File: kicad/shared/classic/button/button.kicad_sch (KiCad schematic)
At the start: 0 parts

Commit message: Draft of Classic button/LED assembly
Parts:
- added D1: LED, LED_THT:LED_D5.0mm, symbol Device:LED
- added J2: Screw_Terminal_01x03, TerminalBlock_Phoenix:TerminalBlock_Phoenix_MKDS-1,5-3-5.08_1x03_P5.08mm_Horizontal, symbol Connector:Screw_Terminal_01x03
- added MX1: MX_SW_HS, PCM_marbastlib-mx:SW_MX_HS_CPG151101S11_1u, symbol marbastlib-mx:MX_SW_HS_CPG151101S11
- added Q1: BC547, Package_TO_SOT_THT:TO-92_Inline, symbol Transistor_BJT:BC547
- added R1: 180, Resistor_SMD:R_0805_2012Metric, symbol Device:R
- added R2: 1.3k, Resistor_SMD:R_0805_2012Metric, symbol Device:R
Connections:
- new net: D1.1 (K), Q1.1 (C)
- new net: D1.2 (A), R1.2
- new net: Q1.2 (B), R2.2
- new net +3V3: J2.1 (Pin_1), MX1.1, R1.1
- new net GND: J2.3 (Pin_3), Q1.3 (E)
- new net SW_OUT: J2.2 (Pin_2), MX1.2, R2.1

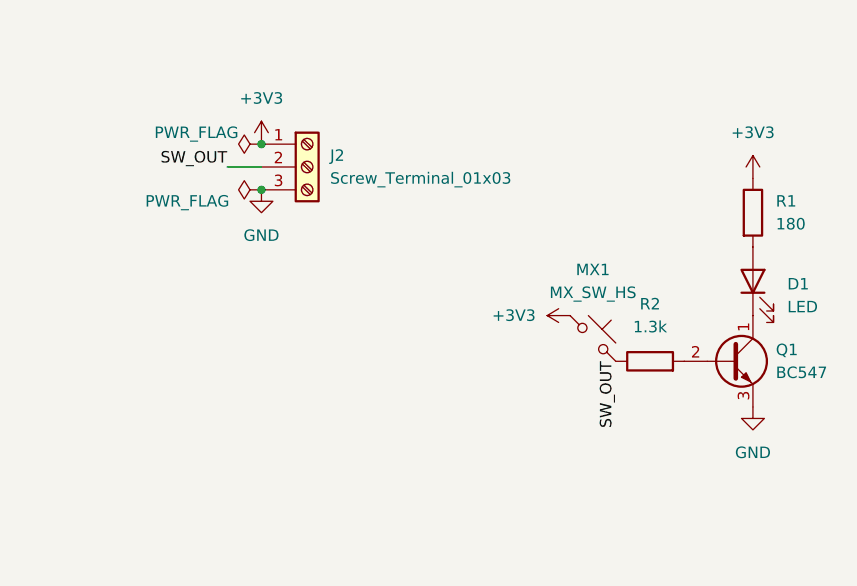
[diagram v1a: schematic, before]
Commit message: Decoupling cap and JST-XA connector for Classic button daughterboard
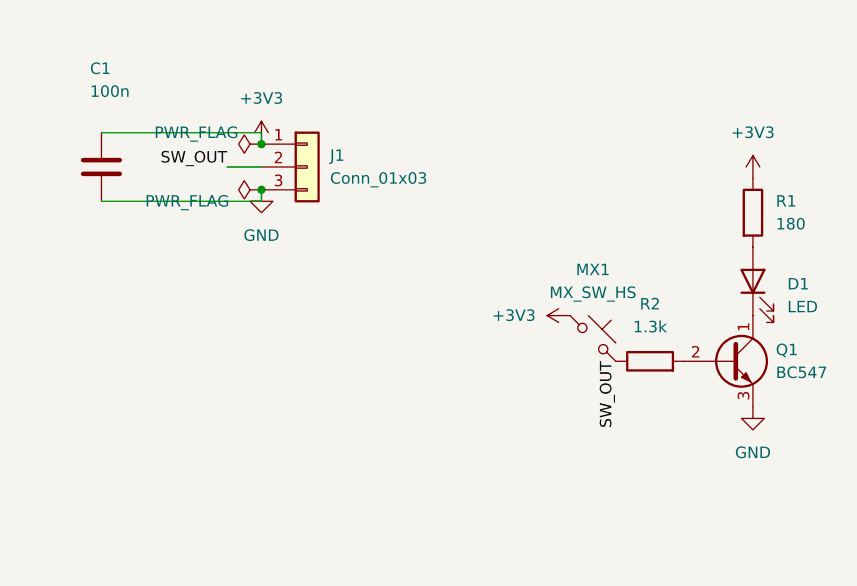
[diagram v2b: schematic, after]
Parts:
- removed J2: Screw_Terminal_01x03, TerminalBlock_Phoenix:TerminalBlock_Phoenix_MKDS-1,5-3-5.08_1x03_P5.08mm_Horizontal, symbol Connector:Screw_Terminal_01x03
- added C1: 100n, Capacitor_SMD:C_0805_2012Metric, symbol Device:C
- added J1: Conn_01x03, Connector_JST:JST_XA_S03B-XASK-1_1x03_P2.50mm_Horizontal, symbol Connector_Generic:Conn_01x03
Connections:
- net +3V3: now also C1.1, J1.1 (Pin_1)
- net GND: now also C1.2, J1.3 (Pin_3)
- net SW_OUT: now also J1.2 (Pin_2)
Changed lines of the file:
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@@
+	(wire
+		(pts
+			(xy 21.59 54.61) (xy 39.37 54.61)
+		)
+		(stroke
+			(width 0)
+			(type default)
+		)
+	)
+	(wire
+		(pts
+			(xy 39.37 60.96) (xy 39.37 62.23)
+		)
+		(stroke
+			(width 0)
+			(type default)
+		)
+	)
+	(wire
+		(pts
+			(xy 39.37 54.61) (xy 39.37 55.88)
+		)
+		(stroke
+			(width 0)
+			(type default)
+		)
+	)
 	(wire
 		(pts
 			(xy 35.56 58.42) (xy 39.37 58.42)
+		)
+		(stroke
+			(width 0)
+			(type default)
+		)
+	)
+	(wire
+		(pts
+			(xy 39.37 62.23) (xy 21.59 62.23)
 		)
 		(stroke
@@
 	)
 	(symbol
+		(lib_id "Device:C")
+		(at 21.59 58.42 0)
+		(unit 1)
+		(body_style 1)
+		(exclude_from_sim no)
+		(in_bom yes)
+		(on_board yes)
+		(in_pos_files yes)
+		(dnp no)
+		(property "Reference" "C1"
+			(at 20.32 47.498 0)
+			(show_name no)
+			(do_not_autoplace no)
+			(effects
+				(font
+					(size 1.27 1.27)
+				)
+				(justify left)
+			)
+		)
+		(property "Value" "100n"
+			(at 20.32 50.038 0)
+			(show_name no)
+			(do_not_autoplace no)
+			(effects
+				(font
+					(size 1.27 1.27)
+				)
+				(justify left)
+			)
+		)
+		(property "Footprint" "Capacitor_SMD:C_0805_2012Metric"
+			(at 22.5552 62.23 0)
+			(hide yes)
+			(show_name no)
+			(do_not_autoplace no)
+			(effects
+				(font
+					(size 1.27 1.27)
+				)
+			)
+		)
+		(property "Datasheet" ""
+			(at 21.59 58.42 0)
+			(hide yes)
+			(show_name no)
+			(do_not_autoplace no)
+			(effects
+				(font
+					(size 1.27 1.27)
+				)
+			)
+		)
+		(property "Description" "Unpolarized capacitor"
+			(at 21.59 58.42 0)
+			(hide yes)
+			(show_name no)
+			(do_not_autoplace no)
+			(effects
+				(font
+					(size 1.27 1.27)
+				)
+			)
+		)
+		(pin "2"
+		)
+		(pin "1"
+		)
+		(instances
+			(project "button"
+				(path "/9bcb4978-1926-4e41-8c2f-efd6bcbfb6f8"
+					(reference "C1")
+					(unit 1)
+				)
+			)
+		)
+	)
+	(symbol
 		(lib_id "Device:LED")
 		(at 93.98 71.12 90)
@@
 	)
 	(symbol
-		(lib_id "Connector:Screw_Terminal_01x03")
-		(at 44.45 58.42 0)
-		(unit 1)
-		(body_style 1)
-		(exclude_from_sim no)
-		(in_bom yes)
-		(on_board yes)
-		(in_pos_files yes)
-		(dnp no)
-		(fields_autoplaced yes)
-		(property "Reference" "J2"
-			(at 46.99 57.1499 0)
-			(show_name no)
-			(do_not_autoplace no)
-			(effects
-				(font
-					(size 1.27 1.27)
-				)
-				(justify left)
-			)
-		)
-		(property "Value" "Screw_Terminal_01x03"
-			(at 46.99 59.6899 0)
-			(show_name no)
-			(do_not_autoplace no)
-			(effects
-				(font
-					(size 1.27 1.27)
-				)
-				(justify left)
-			)
-		)
-		(property "Footprint" "TerminalBlock_Phoenix:TerminalBlock_Phoenix_MKDS-1,5-3-5.08_1x03_P5.08mm_Horizontal"
-			(at 44.45 58.42 0)
-			(hide yes)
-			(show_name no)
-			(do_not_autoplace no)
-			(effects
-				(font
-					(size 1.27 1.27)
-				)
-			)
-		)
-		(property "Datasheet" ""
-			(at 44.45 58.42 0)
-			(hide yes)
-			(show_name no)
-			(do_not_autoplace no)
-			(effects
-				(font
-					(size 1.27 1.27)
-				)
-			)
-		)
-		(property "Description" "Generic screw terminal, single row, 01x03, script generated (kicad-library-utils/schlib/autogen/connector/)"
-			(at 44.45 58.42 0)
-			(hide yes)
-			(show_name no)
-			(do_not_autoplace no)
-			(effects
-				(font
-					(size 1.27 1.27)
-				)
-			)
-		)
-		(pin "3"
-		)
-		(pin "1"
-		)
-		(pin "2"
-		)
-		(instances
-			(project "button"
-				(path "/9bcb4978-1926-4e41-8c2f-efd6bcbfb6f8"
-					(reference "J2")
-					(unit 1)
-				)
-			)
-		)
-	)
-	(symbol
 		(lib_id "power:+3V3")
 		(at 93.98 59.69 0)
@@
 					(unit 1)
 				)
+			)
+		)
+	)
+	(symbol
+		(lib_id "Connector_Generic:Conn_01x03")
+		(at 44.45 58.42 0)
+		(unit 1)
+		(body_style 1)
+		(exclude_from_sim no)
+		(in_bom yes)
+		(on_board yes)
+		(in_pos_files yes)
+		(dnp no)
+		(fields_autoplaced yes)
+		(property "Reference" "J1"
+			(at 46.99 57.1499 0)
+			(show_name no)
+			(do_not_autoplace no)
+			(effects
+				(font
+					(size 1.27 1.27)
+				)
+				(justify left)
+			)
+		)
+		(property "Value" "Conn_01x03"
+			(at 46.99 59.6899 0)
+			(show_name no)
+			(do_not_autoplace no)
+			(effects
+				(font
+					(size 1.27 1.27)
+				)
+				(justify left)
+			)
+		)
+		(property "Footprint" "Connector_JST:JST_XA_S03B-XASK-1_1x03_P2.50mm_Horizontal"
+			(at 44.45 58.42 0)
+			(hide yes)
+			(show_name no)
+			(do_not_autoplace no)
+			(effects
+				(font
+					(size 1.27 1.27)
+				)
+			)
+		)
+		(property "Datasheet" ""
+			(at 44.45 58.42 0)
+			(hide yes)
+			(show_name no)
+			(do_not_autoplace no)
+			(effects
+				(font
+					(size 1.27 1.27)
+				)
+			)
+		)
+		(property "Description" "Generic connector, single row, 01x03, script generated (kicad-library-utils/schlib/autogen/connector/)"
+			(at 44.45 58.42 0)
+			(hide yes)
+			(show_name no)
+			(do_not_autoplace no)
+			(effects
+				(font
+					(size 1.27 1.27)
+				)
+			)
+		)
+		(pin "3"
+		)
+		(pin "2"
+		)
+		(pin "1"
+		)
+		(instances
+			(project "button"
+				(path "/9bcb4978-1926-4e41-8c2f-efd6bcbfb6f8"
+					(reference "J1")
+					(unit 1)
+				)

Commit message: Pulldown for the switch bc I'm dumb
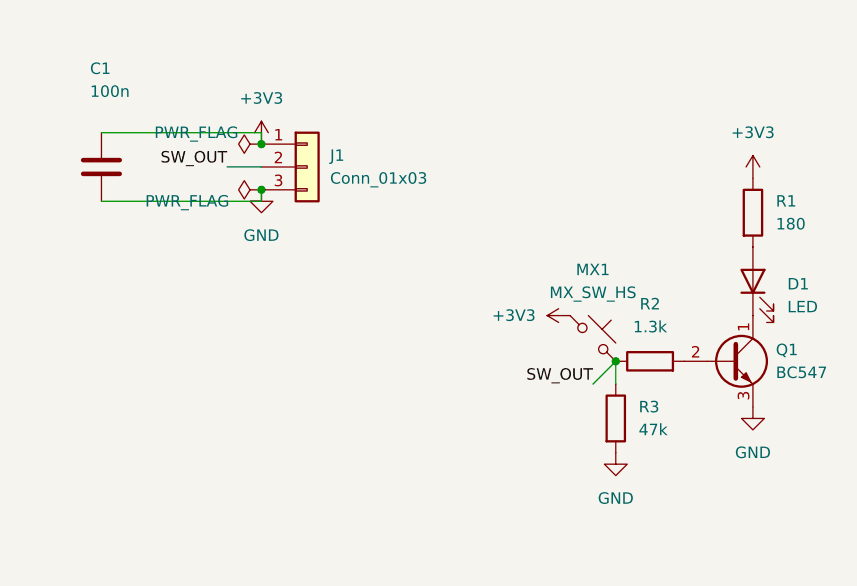
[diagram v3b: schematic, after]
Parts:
- added R3: 47k, Resistor_SMD:R_0805_2012Metric, symbol Device:R
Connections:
- net GND: now also R3.2
- net SW_OUT: now also R3.1
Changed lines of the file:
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@@
+		(color 0 0 0 0)
+	)
+	(junction
+		(at 78.74 80.01)
+		(diameter 0)
 		(color 0 0 0 0)
 	)
@@
 	(wire
 		(pts
-			(xy 35.56 58.42) (xy 39.37 58.42)
+			(xy 76.2 82.55) (xy 78.74 80.01)
 		)
 		(stroke
@@
 	(wire
 		(pts
-			(xy 39.37 62.23) (xy 21.59 62.23)
+			(xy 78.74 80.01) (xy 78.74 82.55)
 		)
 		(stroke
@@
 		)
 	)
+	(wire
+		(pts
+			(xy 35.56 58.42) (xy 39.37 58.42)
+		)
+		(stroke
+			(width 0)
+			(type default)
+		)
+	)
+	(wire
+		(pts
+			(xy 39.37 62.23) (xy 21.59 62.23)
+		)
+		(stroke
+			(width 0)
+			(type default)
+		)
+	)
 	(label "SW_OUT"
-		(at 78.74 80.01 270)
+		(at 76.2 82.55 180)
 		(effects
 			(font
@@
 				(path "/9bcb4978-1926-4e41-8c2f-efd6bcbfb6f8"
 					(reference "#FLG01")
+					(unit 1)
+				)
+			)
+		)
+	)
+	(symbol
+		(lib_id "power:GND")
+		(at 78.74 90.17 0)
+		(unit 1)
+		(body_style 1)
+		(exclude_from_sim no)
+		(in_bom yes)
+		(on_board yes)
+		(in_pos_files yes)
+		(dnp no)
+		(fields_autoplaced yes)
+		(property "Reference" "#PWR06"
+			(at 78.74 96.52 0)
+			(hide yes)
+			(show_name no)
+			(do_not_autoplace no)
+			(effects
+				(font
+					(size 1.27 1.27)
+				)
+			)
+		)
+		(property "Value" "GND"
+			(at 78.74 95.25 0)
+			(show_name no)
+			(do_not_autoplace no)
+			(effects
+				(font
+					(size 1.27 1.27)
+				)
+			)
+		)
+		(property "Footprint" ""
+			(at 78.74 90.17 0)
+			(hide yes)
+			(show_name no)
+			(do_not_autoplace no)
+			(effects
+				(font
+					(size 1.27 1.27)
+				)
+			)
+		)
+		(property "Datasheet" ""
+			(at 78.74 90.17 0)
+			(hide yes)
+			(show_name no)
+			(do_not_autoplace no)
+			(effects
+				(font
+					(size 1.27 1.27)
+				)
+			)
+		)
+		(property "Description" "Power symbol creates a global label with name \"GND\" , ground"
+			(at 78.74 90.17 0)
+			(hide yes)
+			(show_name no)
+			(do_not_autoplace no)
+			(effects
+				(font
+					(size 1.27 1.27)
+				)
+			)
+		)
+		(pin "1"
+		)
+		(instances
+			(project "button"
+				(path "/9bcb4978-1926-4e41-8c2f-efd6bcbfb6f8"
+					(reference "#PWR06")
 					(unit 1)
 				)
@@
 					(unit 1)
 				)
+			)
+		)
+	)
+	(symbol
+		(lib_id "Device:R")
+		(at 78.74 86.36 0)
+		(unit 1)
+		(body_style 1)
+		(exclude_from_sim no)
+		(in_bom yes)
+		(on_board yes)
+		(in_pos_files yes)
+		(dnp no)
+		(fields_autoplaced yes)
+		(property "Reference" "R3"
+			(at 81.28 85.0899 0)
+			(show_name no)
+			(do_not_autoplace no)
+			(effects
+				(font
+					(size 1.27 1.27)
+				)
+				(justify left)
+			)
+		)
+		(property "Value" "47k"
+			(at 81.28 87.6299 0)
+			(show_name no)
+			(do_not_autoplace no)
+			(effects
+				(font
+					(size 1.27 1.27)
+				)
+				(justify left)
+			)
+		)
+		(property "Footprint" "Resistor_SMD:R_0805_2012Metric"
+			(at 76.962 86.36 90)
+			(hide yes)
+			(show_name no)
+			(do_not_autoplace no)
+			(effects
+				(font
+					(size 1.27 1.27)
+				)
+			)
+		)
+		(property "Datasheet" ""
+			(at 78.74 86.36 0)
+			(hide yes)
+			(show_name no)
+			(do_not_autoplace no)
+			(effects
+				(font
+					(size 1.27 1.27)
+				)
+			)
+		)
+		(property "Description" "Resistor"
+			(at 78.74 86.36 0)
+			(hide yes)
+			(show_name no)
+			(do_not_autoplace no)
+			(effects
+				(font
+					(size 1.27 1.27)
+				)
+			)
+		)
+		(pin "1"
+		)
+		(pin "2"
+		)
+		(instances
+			(project "button"
+				(path "/9bcb4978-1926-4e41-8c2f-efd6bcbfb6f8"
+					(reference "R3")
+					(unit 1)
+				)

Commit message: Button/LED assembly Classic actually does the thing properly now
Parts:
- removed J1: Conn_01x03, Connector_JST:JST_XA_S03B-XASK-1_1x03_P2.50mm_Horizontal, symbol Connector_Generic:Conn_01x03
- added J2: Conn_01x04, Connector_JST:JST_XA_B04B-XASK-1-A_1x04_P2.50mm_Vertical, symbol Connector_Generic:Conn_01x04
- added R4: R, Resistor_SMD:R_0805_2012Metric, symbol Device:R
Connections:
- net +3V3: now also J2.1 (Pin_1)
- net GND: now also J2.4 (Pin_4), R4.2
- net SW_OUT: now also J2.2 (Pin_2), R4.1; no longer R2.1, R3.1
- new net LED_IN: J2.3 (Pin_3), R2.1, R3.1
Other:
- moved on the sheet: C1, MX1

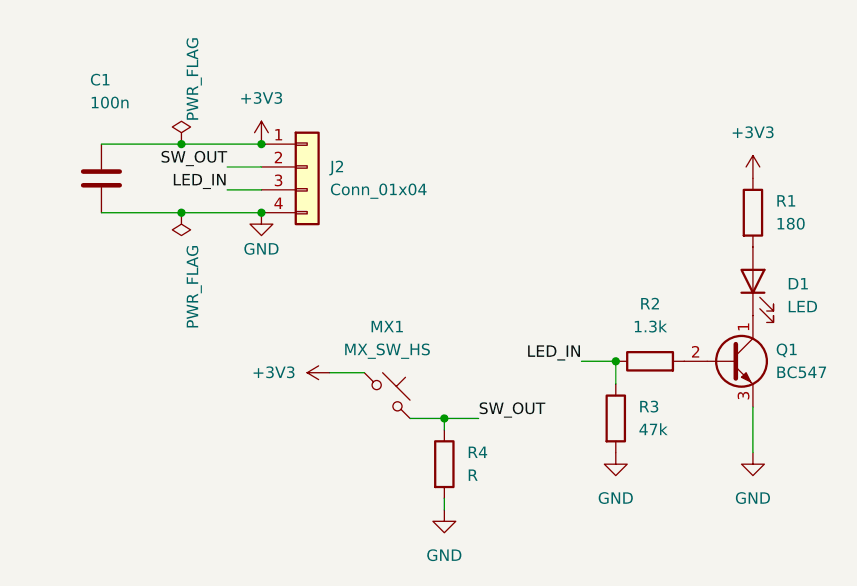
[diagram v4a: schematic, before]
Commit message: feat: Cleaned up pin arrangement for Classic button/LED assembly, added connector for that on Classic control unit main board, added pins for STM32 TODO
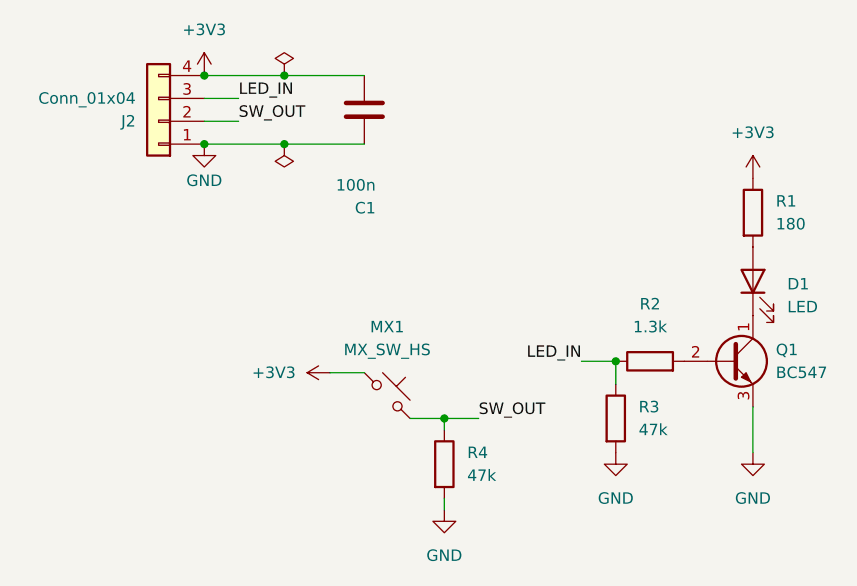
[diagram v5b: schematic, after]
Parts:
- R4: value R -> 47k
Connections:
- net +3V3: now also C1.2, J2.4 (Pin_4); no longer C1.1, J2.1 (Pin_1)
- net GND: now also C1.1, J2.1 (Pin_1); no longer C1.2, J2.4 (Pin_4)
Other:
- moved on the sheet: C1, J2

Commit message: feat: Added main Classic buzzer board; now basically just waiting on XLR5 and HW-0519 footprints; also need to see if I need a separate earth for the HW-0519s on the buzzer boards
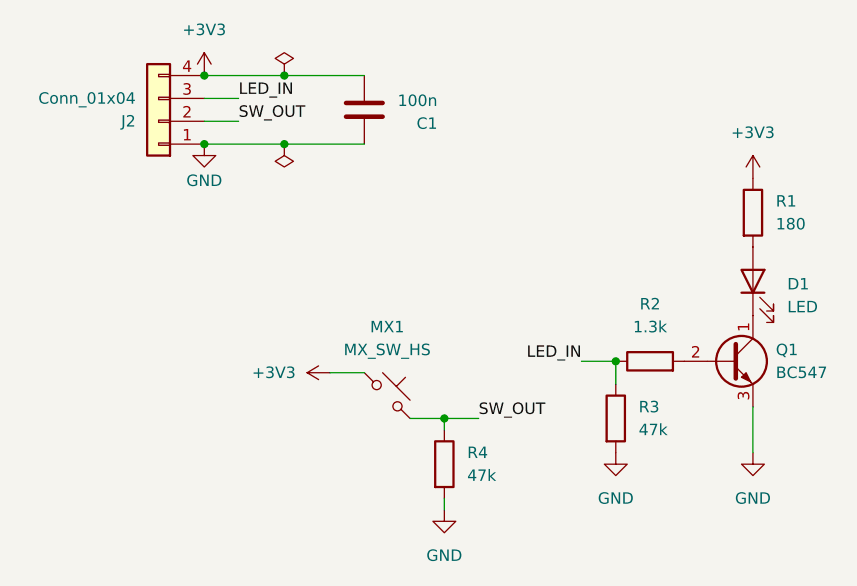
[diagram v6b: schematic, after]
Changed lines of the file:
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@@
+	)
+	(junction
+		(at 33.02 48.26)
+		(diameter 0)
+		(color 0 0 0 0)
 	)
 	(junction
@@
 	)
 	(junction
-		(at 33.02 48.26)
-		(diameter 0)
-		(color 0 0 0 0)
-	)
-	(junction
 		(at 78.74 80.01)
 		(diameter 0)
@@
 	(wire
 		(pts
-			(xy 41.91 55.88) (xy 33.02 55.88)
+			(xy 33.02 55.88) (xy 41.91 55.88)
 		)
 		(stroke
@@
 	(wire
 		(pts
-			(xy 50.8 55.88) (xy 41.91 55.88)
-		)
-		(stroke
-			(width 0)
-			(type default)
-		)
-	)
-	(wire
-		(pts
 			(xy 59.69 95.25) (xy 59.69 96.52)
 		)
@@
 		(pts
 			(xy 59.69 86.36) (xy 59.69 87.63)
+		)
+		(stroke
+			(width 0)
+			(type default)
+		)
+	)
+	(wire
+		(pts
+			(xy 41.91 55.88) (xy 50.8 55.88)
 		)
 		(stroke
@@
 	)
 	(symbol
+		(lib_id "power:PWR_FLAG")
+		(at 41.91 55.88 180)
+		(unit 1)
+		(body_style 1)
+		(exclude_from_sim no)
+		(in_bom yes)
+		(on_board yes)
+		(in_pos_files yes)
+		(dnp no)
+		(fields_autoplaced yes)
+		(property "Reference" "#FLG02"
+			(at 41.91 57.785 0)
+			(hide yes)
+			(show_name no)
+			(do_not_autoplace no)
+			(effects
+				(font
+					(size 1.27 1.27)
+				)
+			)
+		)
+		(property "Value" "PWR_FLAG"
+			(at 41.91 60.96 0)
+			(hide yes)
+			(show_name no)
+			(do_not_autoplace no)
+			(effects
+				(font
+					(size 1.27 1.27)
+				)
+			)
+		)
+		(property "Footprint" ""
+			(at 41.91 55.88 0)
+			(hide yes)
+			(show_name no)
+			(do_not_autoplace no)
+			(effects
+				(font
+					(size 1.27 1.27)
+				)
+			)
+		)
+		(property "Datasheet" ""
+			(at 41.91 55.88 0)
+			(hide yes)
+			(show_name no)
+			(do_not_autoplace no)
+			(effects
+				(font
+					(size 1.27 1.27)
+				)
+			)
+		)
+		(property "Description" "Special symbol for telling ERC where power comes from"
+			(at 41.91 55.88 0)
+			(hide yes)
+			(show_name no)
+			(do_not_autoplace no)
+			(effects
+				(font
+					(size 1.27 1.27)
+				)
+			)
+		)
+		(pin "1"
+		)
+		(instances
+			(project "button"
+				(path "/9bcb4978-1926-4e41-8c2f-efd6bcbfb6f8"
+					(reference "#FLG02")
+					(unit 1)
+				)
+			)
+		)
+	)
+	(symbol
 		(lib_id "Device:C")
 		(at 50.8 52.07 180)
@@
 		(dnp no)
 		(property "Reference" "C1"
-			(at 52.07 62.992 0)
+			(at 58.928 53.594 0)
 			(show_name no)
 			(do_not_autoplace no)
@@
 		)
 		(property "Value" "100n"
-			(at 52.07 60.452 0)
+			(at 58.928 51.054 0)
 			(show_name no)
 			(do_not_autoplace no)
@@
 					(unit 1)
 				)
-			)
-		)
-	)
-	(symbol
-		(lib_id "power:PWR_FLAG")
-		(at 41.91 55.88 180)
-		(unit 1)
-		(body_style 1)
-		(exclude_from_sim no)
-		(in_bom yes)
-		(on_board yes)
-		(in_pos_files yes)
-		(dnp no)
-		(property "Reference" "#FLG02"
-			(at 41.91 57.785 0)
-			(hide yes)
-			(show_name no)
-			(do_not_autoplace no)
-			(effects
-				(font
-					(size 1.27 1.27)
-				)
-			)
-		)
-		(property "Value" "PWR_FLAG"
-			(at 40.64 58.42 90)
-			(hide yes)
-			(show_name no)
-			(do_not_autoplace no)
-			(effects
-				(font
-					(size 1.27 1.27)
-				)
-				(justify left)
-			)
-		)
-		(property "Footprint" ""
-			(at 41.91 55.88 0)
-			(hide yes)
-			(show_name no)
-			(do_not_autoplace no)
-			(effects
-				(font
-					(size 1.27 1.27)
-				)
-			)
-		)
-		(property "Datasheet" ""
-			(at 41.91 55.88 0)
-			(hide yes)
-			(show_name no)
-			(do_not_autoplace no)
-			(effects
-				(font
-					(size 1.27 1.27)
-				)
-			)
-		)
-		(property "Description" "Special symbol for telling ERC where power comes from"
-			(at 41.91 55.88 0)
-			(hide yes)
-			(show_name no)
-			(do_not_autoplace no)
-			(effects
-				(font
-					(size 1.27 1.27)
-				)
-			)
-		)
-		(pin "1"
-		)
-		(instances
-			(project "button"
-				(path "/9bcb4978-1926-4e41-8c2f-efd6bcbfb6f8"
-					(reference "#FLG02")
-					(unit 1)
-				)
